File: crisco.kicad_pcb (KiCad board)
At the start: 2 copper layers, 213.4 x 38.1 mm, 44 parts

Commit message: bus routing'
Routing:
- net col9: track 228.8 -> 226.9 mm
- net col3: track 93.1 -> 92.1 mm
- net col4: track 109.7 -> 110.5 mm
- net col1: track 63.3 -> 62.6 mm
- net col2: track 71.4 -> 72.0 mm

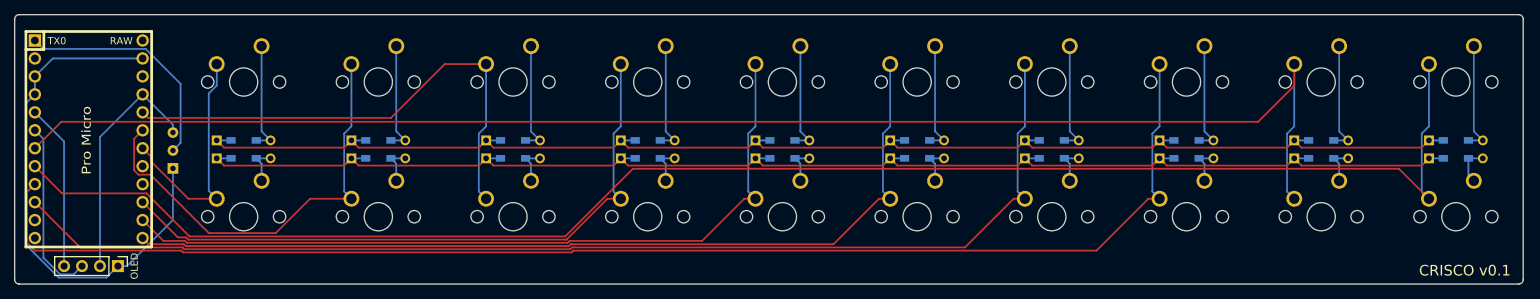
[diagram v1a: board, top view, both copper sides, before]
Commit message: added pullup resistors, bom, and instructions
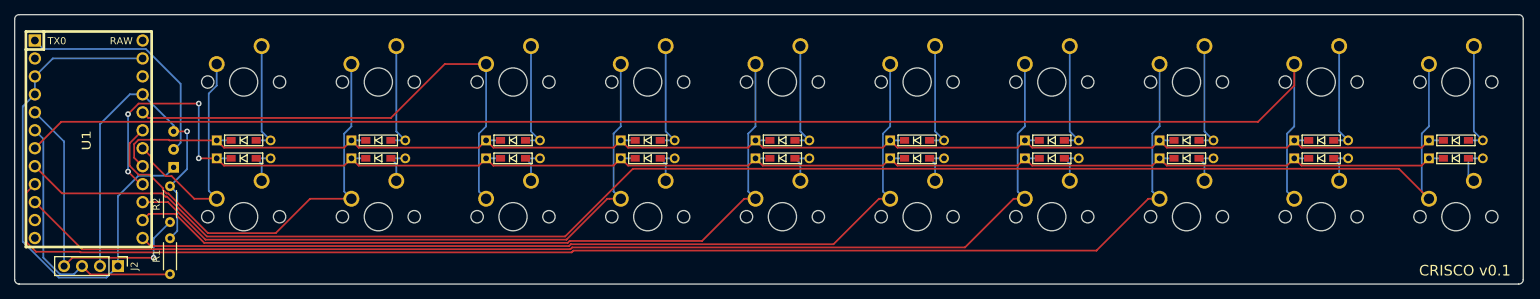
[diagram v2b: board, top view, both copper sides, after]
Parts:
- added R1: R_US, Resistor_THT:R_Axial_DIN0204_L3.6mm_D1.6mm_P5.08mm_Horizontal, F.Cu at (42.3, 105.3)
- added R2: R_US, Resistor_THT:R_Axial_DIN0204_L3.6mm_D1.6mm_P5.08mm_Horizontal, F.Cu at (42.3, 97.9)
- D1, D10, D11, D12, D13, D14, D15, D16, D17, D18, D19, D2, D20, D3, D4, D5, D6, D7, D8, D9: moved to F.Cu
- U1: renamed from Pro Micro
- moved J1 0.19 mm to (42.8, 87.6)
- renumbered LED to J1, OLED to J2
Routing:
- net row1: track 199.4 -> 231.3 mm, vias 0 -> 4
- net VCC: track 34.0 -> 53.9 mm, vias 0 -> 1
- net sda: track 23.5 -> 42.6 mm, vias 0 -> 1
- net row0: track 199.7 -> 215.3 mm
- net scl: track 25.5 -> 38.6 mm
- net GND: track 74.0 -> 75.9 mm
- net col4: track 110.5 -> 111.2 mm
- net col1: track 62.6 -> 63.2 mm

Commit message: update gerber
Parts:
- removed R1, R2: R_US, Resistor_THT:R_Axial_DIN0204_L3.6mm_D1.6mm_P5.08mm_Horizontal
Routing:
- net sda: track 42.6 -> 23.5 mm, vias 1 -> 0
- net VCC: track 53.9 -> 35.3 mm, vias 1 -> 0
- net scl: track 38.6 -> 25.5 mm
